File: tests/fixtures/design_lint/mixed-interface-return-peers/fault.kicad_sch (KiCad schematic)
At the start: 3 parts, among them J1 Synthetic USB port, J2 Synthetic serial port, J3 Synthetic USB port

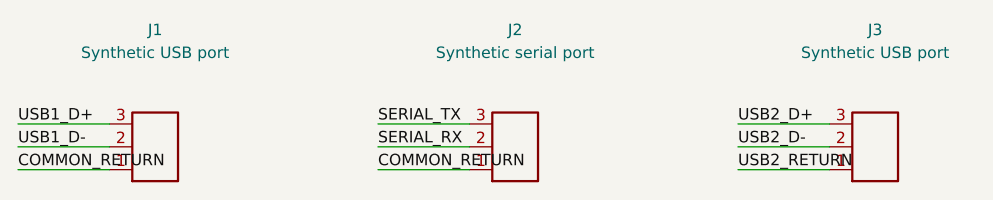
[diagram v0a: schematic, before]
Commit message: fix(lint): align mixed interface fixture pin mapping
Correct synthetic schematic labels so USB D+ and serial TX occupy pin 1 while mapped return roles occupy pin 3. The exact native gate caught the fixture's coordinate reversal on both KiCad versions.

Lint-Rule: connector.repeated_pin_function
Native-Fixture: KICAD_RUN_NATIVE_DB9_RETURN_CONTRACT_FIXTURES
Native-Fixture: KICAD_RUN_NATIVE_MIXED_INTERFACE_RETURN_FIXTURES
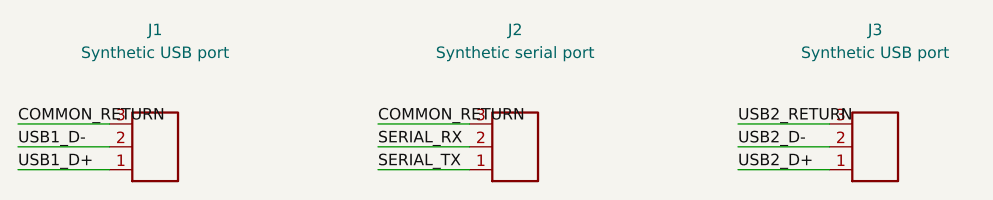
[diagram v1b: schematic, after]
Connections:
- net COMMON_RETURN: now also J1.3 (GND), J2.3 (Pin_3); no longer J1.1 (D+), J2.1 (TX)
- net SERIAL_TX: now also J2.1 (TX); no longer J2.3 (Pin_3)
- net USB1_D+: now also J1.1 (D+); no longer J1.3 (GND)
- net USB2_D+: now also J3.1 (D+); no longer J3.3 (GND)
- net USB2_RETURN: now also J3.3 (GND); no longer J3.1 (D+)
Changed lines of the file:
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@@
     (instances (project "synthetic-mixed-interface-return-peers" (path "/85000000-0000-4000-8000-000000000001" (reference "J3") (unit 1)))))
   (wire (pts (xy 84.92 77.46) (xy 74.76 77.46)) (stroke (width 0) (type default)))
-  (label "USB1_D+" (at 74.76 77.46 0) (effects (font (size 1.27 1.27)) (justify left bottom)))
+  (label "COMMON_RETURN" (at 74.76 77.46 0) (effects (font (size 1.27 1.27)) (justify left bottom)))
   (wire (pts (xy 84.92 80) (xy 74.76 80)) (stroke (width 0) (type default)))
   (label "USB1_D-" (at 74.76 80 0) (effects (font (size 1.27 1.27)) (justify left bottom)))
   (wire (pts (xy 84.92 82.54) (xy 74.76 82.54)) (stroke (width 0) (type default)))
-  (label "COMMON_RETURN" (at 74.76 82.54 0) (effects (font (size 1.27 1.27)) (justify left bottom)))
+  (label "USB1_D+" (at 74.76 82.54 0) (effects (font (size 1.27 1.27)) (justify left bottom)))
   (wire (pts (xy 124.92 77.46) (xy 114.76 77.46)) (stroke (width 0) (type default)))
-  (label "SERIAL_TX" (at 114.76 77.46 0) (effects (font (size 1.27 1.27)) (justify left bottom)))
+  (label "COMMON_RETURN" (at 114.76 77.46 0) (effects (font (size 1.27 1.27)) (justify left bottom)))
   (wire (pts (xy 124.92 80) (xy 114.76 80)) (stroke (width 0) (type default)))
   (label "SERIAL_RX" (at 114.76 80 0) (effects (font (size 1.27 1.27)) (justify left bottom)))
   (wire (pts (xy 124.92 82.54) (xy 114.76 82.54)) (stroke (width 0) (type default)))
-  (label "COMMON_RETURN" (at 114.76 82.54 0) (effects (font (size 1.27 1.27)) (justify left bottom)))
+  (label "SERIAL_TX" (at 114.76 82.54 0) (effects (font (size 1.27 1.27)) (justify left bottom)))
   (wire (pts (xy 164.92 77.46) (xy 154.76 77.46)) (stroke (width 0) (type default)))
-  (label "USB2_D+" (at 154.76 77.46 0) (effects (font (size 1.27 1.27)) (justify left bottom)))
+  (label "USB2_RETURN" (at 154.76 77.46 0) (effects (font (size 1.27 1.27)) (justify left bottom)))
   (wire (pts (xy 164.92 80) (xy 154.76 80)) (stroke (width 0) (type default)))
   (label "USB2_D-" (at 154.76 80 0) (effects (font (size 1.27 1.27)) (justify left bottom)))
   (wire (pts (xy 164.92 82.54) (xy 154.76 82.54)) (stroke (width 0) (type default)))
-  (label "USB2_RETURN" (at 154.76 82.54 0) (effects (font (size 1.27 1.27)) (justify left bottom)))
+  (label "USB2_D+" (at 154.76 82.54 0) (effects (font (size 1.27 1.27)) (justify left bottom)))
   (sheet_instances (path "/" (page "1")))
 )
